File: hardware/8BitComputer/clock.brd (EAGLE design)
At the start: 100 x 75 mm, 29 parts, among them IC1 LM555CN, J1 Power, J2 Power, J3 CLK_OUTS, Q1 P2N2222AZL1G, Q2 P2N2222AZL1G

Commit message: updated brd
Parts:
- C2: device passives:C075-032X103 -> passives:C0805K
- R5: device passives:AXIAL-0.3 -> passives:0805
- moved R7 8.80 mm to (72.5, 12.1), flipped to the bottom, turned to 0 degrees
- moved R9 4.35 mm to (66.9, 48.5), flipped to the bottom, turned to 180 degrees
- moved R1 3.02 mm to (22.4, 35.2), flipped to the bottom
- moved C6 2.29 mm to (73.0, 24.3), flipped to the bottom, turned to 0 degrees
- moved C5 1.70 mm to (59.8, 37.2), flipped to the bottom, turned to 90 degrees
- moved R8 1.02 mm to (81.2, 38.1), flipped to the bottom, turned to 0 degrees
- flipped C1 to the bottom
- flipped C2 to the bottom
- flipped C3 to the bottom
- flipped C4 to the bottom
- flipped R2 to the bottom
- flipped R3 to the bottom
- flipped R4 to the bottom
- flipped R5 to the bottom
- flipped R6 to the bottom
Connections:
- net N$6: now also R5.1; no longer R5.P$1
- net VCC5V: now also R5.2; no longer R5.P$2
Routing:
- net GND: track 79.0 -> 43.8 mm
- net CLOCK_OUT: track 59.9 -> 51.0 mm
- net N$7: track 15.8 -> 10.9 mm
- net MANUAL_TIMER: track 42.4 -> 39.1 mm
- net SWITCHED_CLOCK_OUT: track 17.1 -> 19.9 mm
- net N$6: track 13.5 -> 16.0 mm
- net 555-1-OUT: track 54.1 -> 52.6 mm
- net N$1: track 4.71 -> 3.31 mm
- net N$12: track 16.6 -> 17.8 mm
- net N$2: track 6.13 -> 7.38 mm
- net VCC5V: track 287.5 -> 288.6 mm
- net N$8: track 7.92 -> 6.85 mm
- added copper zone on layer 1, net NOTHING
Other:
- board text added: "555 MANUAL"
- board text added: "HALT CLOCK"
- board text added: "MANUAL CLOCK"
- board text removed: "555 Manual"
- board text removed: "HALT CPU"

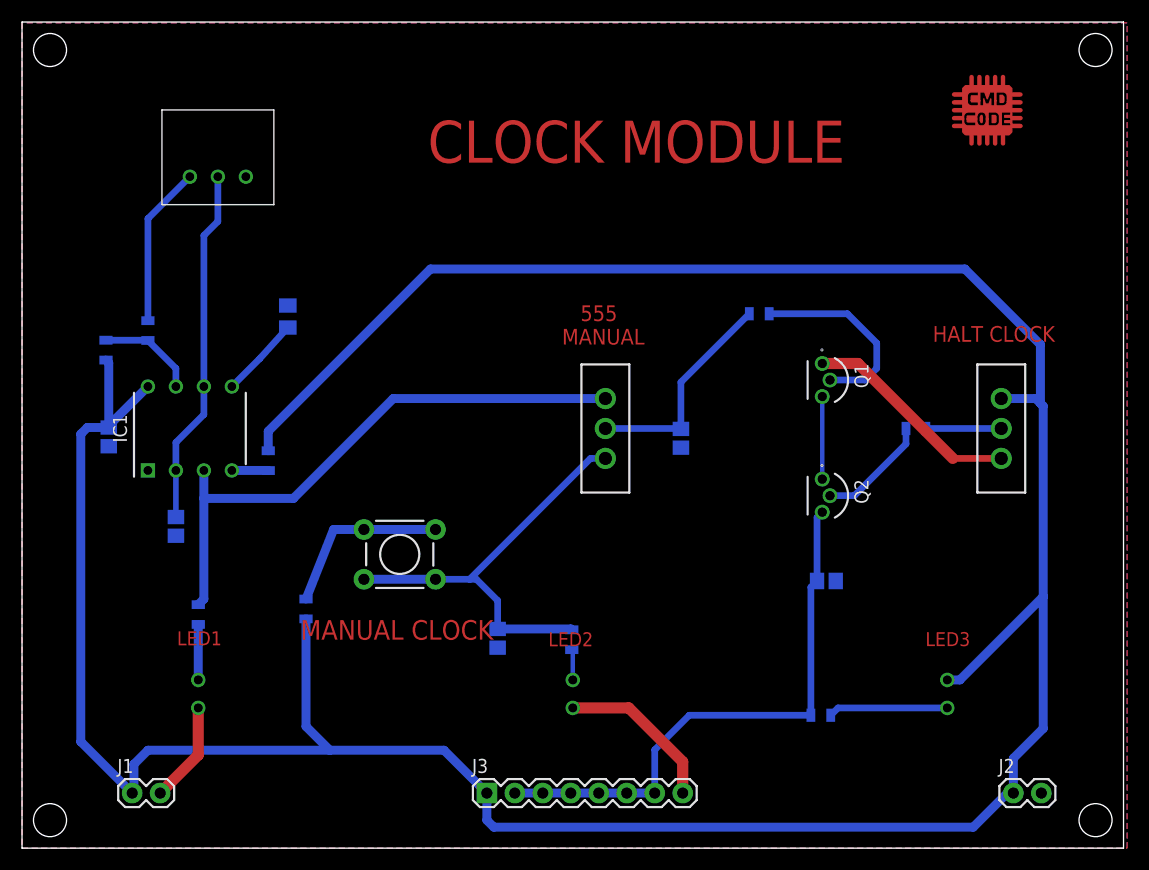
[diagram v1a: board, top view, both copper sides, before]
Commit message: fixed clock module so it should actually work now
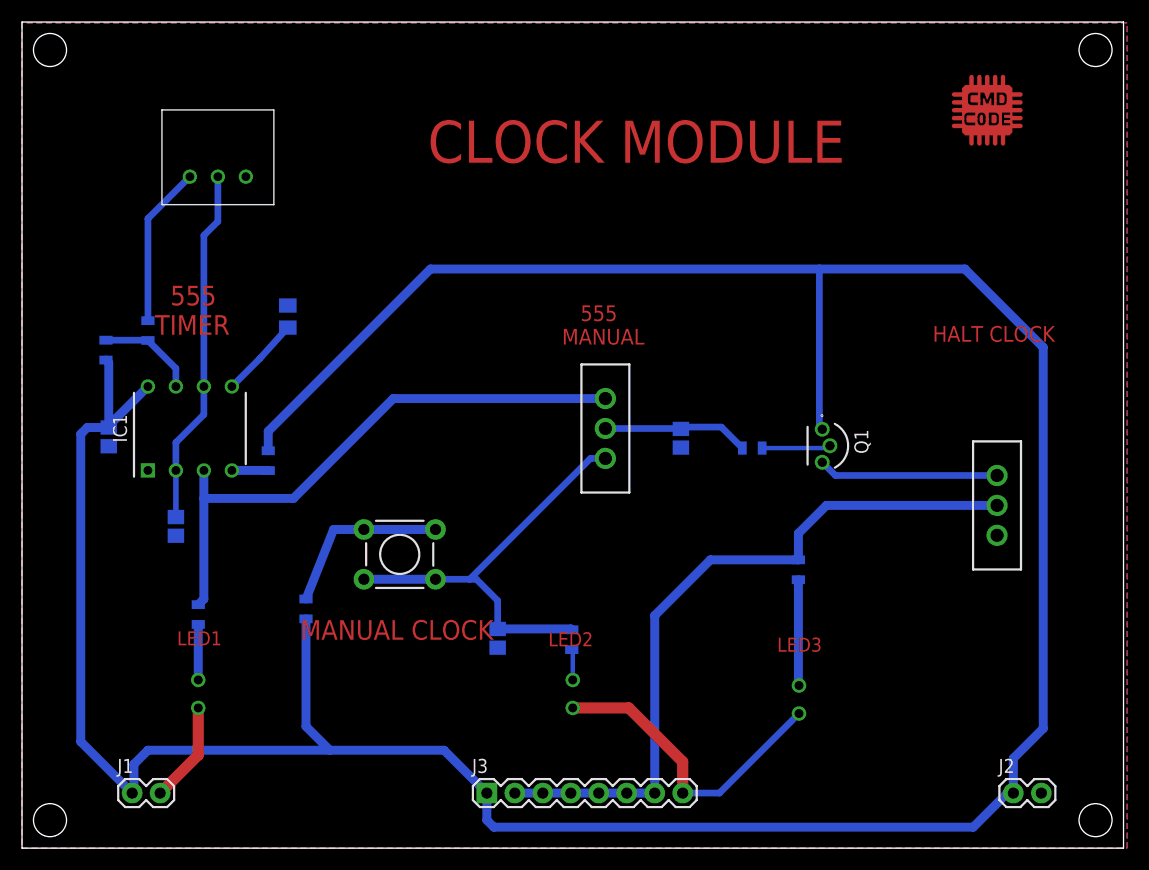
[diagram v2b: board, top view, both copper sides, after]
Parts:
- removed C6: 0.1 uF, passives:C0805
- removed Q2: P2N2222AZL1G, transitors:2N6027
- removed R8: 1 K, passives:0805
- moved LED3 13.5 mm to (70.5, 13.5)
- moved R7 13.4 mm to (70.5, 25.3), turned to 90 degrees
- moved R9 12.2 mm to (66.3, 36.3)
- moved S2 7.00 mm to (88.5, 31.1), turned to 0 degrees
- moved Q1 5.97 mm to (75.0, 36.5)
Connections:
- removed net N$8: R8.1, S2.2
- removed net N$9: Q2.2, R8.2
- net CLOCK_OUT: now also S2.2; no longer C6.2, Q2.3
- net GND: now also LED3.K, S2.3; no longer C6.1, Q1.1, S2.1
- net N$10: now also S2.1; no longer Q2.1
- net N$7: now also LED3.A; no longer LED3.K
- net VCC5V: now also Q1.1; no longer LED3.A, S2.3
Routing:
- net CLOCK_OUT: track 51.0 -> 65.4 mm
- net N$12: track 17.8 -> 6.24 mm
- net N$9: track 10.3 -> 0.00 mm
- net N$10: track 7.50 -> 16.4 mm
- net N$8: track 6.85 -> 0.00 mm
- net SWITCHED_CLOCK_OUT: track 19.9 -> 13.3 mm
- net GND: track 43.8 -> 37.6 mm
- net N$7: track 10.9 -> 9.63 mm
- net VCC5V: track 288.6 -> 287.6 mm
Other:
- board text added: "555 TIMER"
